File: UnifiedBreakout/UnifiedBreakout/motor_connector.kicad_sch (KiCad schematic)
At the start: 1 part, among them J7 RJ45

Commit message: WIP updating breakout for electrical enclosure
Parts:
- J7: symbol UnifiedBreakout-rescue:RJ45-Connector -> Connector:RJ45
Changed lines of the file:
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@@
-(kicad_sch (version 20211123) (generator eeschema)
+(kicad_sch (version 20230121) (generator eeschema)
   (paper "A4")
   (junction (at 121.92 92.71) (diameter 0.9144) (color 0 0 0 0)
@@
   )
   (wire (pts (xy 127 90.17) (xy 88.9 90.17))
-    (stroke (width 0) (type solid) (color 0 0 0 0))
+    (stroke (width 0) (type solid))
   )
   (wire (pts (xy 127 82.55) (xy 121.92 82.55))
-    (stroke (width 0) (type solid) (color 0 0 0 0))
+    (stroke (width 0) (type solid))
   )
   (wire (pts (xy 121.92 77.47) (xy 121.92 82.55))
-    (stroke (width 0) (type solid) (color 0 0 0 0))
+    (stroke (width 0) (type solid))
   )
   (wire (pts (xy 121.92 92.71) (xy 121.92 101.6))
-    (stroke (width 0) (type solid) (color 0 0 0 0))
+    (stroke (width 0) (type solid))
   )
   (wire (pts (xy 127 95.25) (xy 88.9 95.25))
-    (stroke (width 0) (type solid) (color 0 0 0 0))
+    (stroke (width 0) (type solid))
   )
   (wire (pts (xy 127 80.01) (xy 88.9 80.01))
-    (stroke (width 0) (type solid) (color 0 0 0 0))
+    (stroke (width 0) (type solid))
   )
   (wire (pts (xy 127 77.47) (xy 121.92 77.47))
-    (stroke (width 0) (type solid) (color 0 0 0 0))
+    (stroke (width 0) (type solid))
   )
   (wire (pts (xy 121.92 87.63) (xy 121.92 92.71))
-    (stroke (width 0) (type solid) (color 0 0 0 0))
+    (stroke (width 0) (type solid))
   )
   (wire (pts (xy 121.92 82.55) (xy 121.92 87.63))
-    (stroke (width 0) (type solid) (color 0 0 0 0))
+    (stroke (width 0) (type solid))
   )
   (wire (pts (xy 127 87.63) (xy 121.92 87.63))
-    (stroke (width 0) (type solid) (color 0 0 0 0))
+    (stroke (width 0) (type solid))
   )
   (wire (pts (xy 127 85.09) (xy 88.9 85.09))
-    (stroke (width 0) (type solid) (color 0 0 0 0))
+    (stroke (width 0) (type solid))
   )
   (wire (pts (xy 127 92.71) (xy 121.92 92.71))
-    (stroke (width 0) (type solid) (color 0 0 0 0))
+    (stroke (width 0) (type solid))
   )
-  (hierarchical_label "ENABLE" (shape input) (at 88.9 90.17 180)
+  (hierarchical_label "ENABLE" (shape input) (at 88.9 90.17 180) (fields_autoplaced)
     (effects (font (size 1.27 1.27)) (justify right))
   )
-  (hierarchical_label "ALARM" (shape input) (at 88.9 95.25 180)
+  (hierarchical_label "ALARM" (shape input) (at 88.9 95.25 180) (fields_autoplaced)
     (effects (font (size 1.27 1.27)) (justify right))
   )
-  (hierarchical_label "STEP" (shape input) (at 88.9 80.01 180)
+  (hierarchical_label "STEP" (shape input) (at 88.9 80.01 180) (fields_autoplaced)
     (effects (font (size 1.27 1.27)) (justify right))
   )
-  (hierarchical_label "DIR" (shape input) (at 88.9 85.09 180)
+  (hierarchical_label "DIR" (shape input) (at 88.9 85.09 180) (fields_autoplaced)
     (effects (font (size 1.27 1.27)) (justify right))
   )
-  (hierarchical_label "GND" (shape passive) (at 121.92 101.6 270)
+  (hierarchical_label "GND" (shape passive) (at 121.92 101.6 270) (fields_autoplaced)
     (effects (font (size 1.27 1.27)) (justify right))
   )
-  (symbol (lib_id "UnifiedBreakout-rescue:RJ45-Connector") (at 137.16 85.09 180) (unit 1)
-    (in_bom yes) (on_board yes)
-    (property "Reference" "J7" (id 0) (at 145.542 85.1916 0)
+  (symbol (lib_id "Connector:RJ45") (at 137.16 85.09 180) (unit 1)
+    (in_bom yes) (on_board yes) (dnp no)
+    (property "Reference" "J7" (at 145.542 85.1916 0)
       (effects (font (size 1.27 1.27)) (justify right))
     )
-    (property "Value" "RJ45" (id 1) (at 145.542 87.503 0)
+    (property "Value" "RJ45" (at 145.542 87.503 0)
       (effects (font (size 1.27 1.27)) (justify right))
     )
-    (property "Footprint" "Stewart:SS6488SANF1" (id 2) (at 137.16 85.725 90)
+    (property "Footprint" "Stewart:SS6488SANF1" (at 137.16 85.725 90)
       (effects (font (size 1.27 1.27)) hide)
     )
-    (property "Datasheet" "~" (id 3) (at 137.16 85.725 90)
+    (property "Datasheet" "~" (at 137.16 85.725 90)
       (effects (font (size 1.27 1.27)) hide)
     )
-    (property "MPN" "SS-6488S-A-NF-1" (id 4) (at 137.16 85.09 0)
+    (property "MPN" "SS-6488S-A-NF-1" (at 137.16 85.09 0)
       (effects (font (size 1.27 1.27)) hide)
     )
-    (property "Manufacturer" "Bel" (id 5) (at 137.16 85.09 0)
+    (property "Manufacturer" "Bel" (at 137.16 85.09 0)
+      (effects (font (size 1.27 1.27)) hide)
+    )
+    (property "Farnell PN" "" (at 137.16 85.09 0)
       (effects (font (size 1.27 1.27)) hide)
     )
@@
     (pin "7")
     (pin "8")
+    (instances
+      (project "UnifiedBreakout"
+        (path "/e63e39d7-6ac0-4ffd-8aa3-1841a4541b55/00000000-0000-0000-0000-00005e6754f3"
+          (reference "J7") (unit 1)
+        )
+        (path "/e63e39d7-6ac0-4ffd-8aa3-1841a4541b55/00000000-0000-0000-0000-00005e67fd54"
+          (reference "J8") (unit 1)
+        )
+        (path "/e63e39d7-6ac0-4ffd-8aa3-1841a4541b55/00000000-0000-0000-0000-00005e67ffe4"
+          (reference "J9") (unit 1)
+        )
+      )
+    )
   )
 )

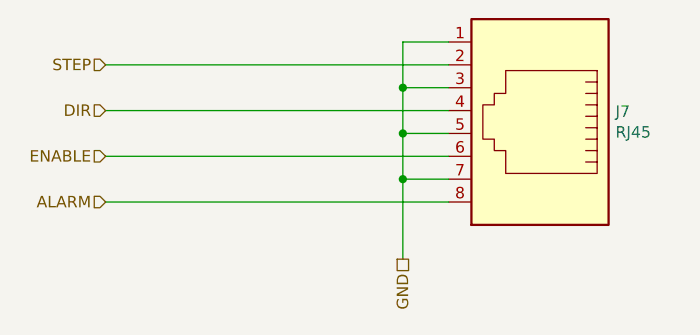
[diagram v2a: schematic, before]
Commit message: Grouped 4 way RJ45s
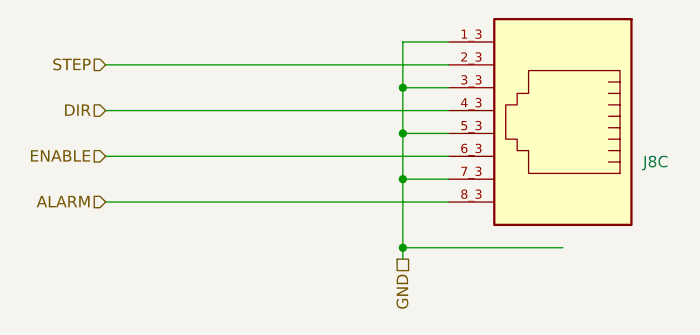
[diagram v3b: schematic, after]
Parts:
- removed J7: RJ45, Stewart:SS6488SANF1, symbol Connector:RJ45
- added J8: (no value), UnifiedBreakout:SS71800-041F, symbol UnifiedBreakout:SS71800-041F
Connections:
- net ALARM: now also J8.8_3 (P8_3)
- net DIR: now also J8.4_3 (P4_3)
- net ENABLE: now also J8.6_3 (P6_3)
- net GND: now also J8.1_3 (P1_3), J8.3_3 (P3_3), J8.5_3 (P5_3), J8.7_3 (P7_3)
- net STEP: now also J8.2_3 (P2_3)
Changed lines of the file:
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@@
   (junction (at 121.92 82.55) (diameter 0.9144) (color 0 0 0 0)
+  )
+  (junction (at 121.92 100.33) (diameter 0) (color 0 0 0 0)
   )
   (junction (at 121.92 87.63) (diameter 0.9144) (color 0 0 0 0)
@@
     (stroke (width 0) (type solid))
   )
-  (wire (pts (xy 121.92 92.71) (xy 121.92 101.6))
+  (wire (pts (xy 121.92 100.33) (xy 139.7 100.33))
+    (stroke (width 0) (type default))
+  )
+  (wire (pts (xy 121.92 92.71) (xy 121.92 100.33))
+    (stroke (width 0) (type solid))
+  )
+  (wire (pts (xy 121.92 100.33) (xy 121.92 101.6))
     (stroke (width 0) (type solid))
   )
@@
     (effects (font (size 1.27 1.27)) (justify right))
   )
-  (symbol (lib_id "Connector:RJ45") (at 137.16 85.09 180) (unit 1)
+  (symbol (lib_id "UnifiedBreakout:SS71800-041F") (at 139.7 86.36 0) (mirror y) (unit 3)
     (in_bom yes) (on_board yes) (dnp no)
-    (property "Reference" "J7" (at 145.542 85.1916 0)
+    (property "Reference" "J8" (at 148.59 90.805 0)
       (effects (font (size 1.27 1.27)) (justify right))
     )
-    (property "Value" "RJ45" (at 145.542 87.503 0)
+    (property "Value" "" (at 148.59 88.265 0)
       (effects (font (size 1.27 1.27)) (justify right))
     )
-    (property "Footprint" "Stewart:SS6488SANF1" (at 137.16 85.725 90)
+    (property "Footprint" "UnifiedBreakout:SS71800-041F" (at 139.7 86.36 0)
+      (effects (font (size 1.27 1.27)) (justify bottom) hide)
+    )
+    (property "Datasheet" "" (at 139.7 86.36 0)
       (effects (font (size 1.27 1.27)) hide)
     )
-    (property "Datasheet" "~" (at 137.16 85.725 90)
-      (effects (font (size 1.27 1.27)) hide)
+    (property "MPN" "SS71800-041F" (at 148.59 85.725 0)
+      (effects (font (size 1.27 1.27)) (justify right) hide)
     )
-    (property "MPN" "SS-6488S-A-NF-1" (at 137.16 85.09 0)
-      (effects (font (size 1.27 1.27)) hide)
+    (property "Manufacturer" "Stewart Connector" (at 148.59 83.185 0)
+      (effects (font (size 1.27 1.27)) (justify right) hide)
     )
-    (property "Manufacturer" "Bel" (at 137.16 85.09 0)
-      (effects (font (size 1.27 1.27)) hide)
+    (property "Farnell PN" "2891045" (at 148.59 80.645 0)
+      (effects (font (size 1.27 1.27)) (justify right) hide)
     )
-    (property "Farnell PN" "" (at 137.16 85.09 0)
-      (effects (font (size 1.27 1.27)) hide)
-    )
-    (pin "1")
-    (pin "2")
-    (pin "3")
-    (pin "4")
-    (pin "5")
-    (pin "6")
-    (pin "7")
-    (pin "8")
+    (pin "1_1")
+    (pin "2_1")
+    (pin "3_1")
+    (pin "4_1")
+    (pin "5_1")
+    (pin "6_1")
+    (pin "7_1")
+    (pin "8_1")
+    (pin "S1")
+    (pin "S2")
+    (pin "S3")
+    (pin "S4")
+    (pin "S5")
+    (pin "1_2")
+    (pin "2_2")
+    (pin "3_2")
+    (pin "4_2")
+    (pin "5_2")
+    (pin "6_2")
+    (pin "7_2")
+    (pin "8_2")
+    (pin "1_3")
+    (pin "2_3")
+    (pin "3_3")
+    (pin "4_3")
+    (pin "5_3")
+    (pin "6_3")
+    (pin "7_3")
+    (pin "8_3")
+    (pin "1_4")
+    (pin "2_4")
+    (pin "3_4")
+    (pin "4_4")
+    (pin "5_4")
+    (pin "6_4")
+    (pin "7_4")
+    (pin "8_4")
     (instances
       (project "UnifiedBreakout"
-        (path "/e63e39d7-6ac0-4ffd-8aa3-1841a4541b55/00000000-0000-0000-0000-00005e6754f3"
-          (reference "J7") (unit 1)
+        (path "/e63e39d7-6ac0-4ffd-8aa3-1841a4541b55/00000000-0000-0000-0000-00005e67ffe4"
+          (reference "J8") (unit 3)
         )
         (path "/e63e39d7-6ac0-4ffd-8aa3-1841a4541b55/00000000-0000-0000-0000-00005e67fd54"
+          (reference "J8") (unit 2)
+        )
+        (path "/e63e39d7-6ac0-4ffd-8aa3-1841a4541b55/00000000-0000-0000-0000-00005e6754f3"
           (reference "J8") (unit 1)
         )
-        (path "/e63e39d7-6ac0-4ffd-8aa3-1841a4541b55/00000000-0000-0000-0000-00005e67ffe4"
-          (reference "J9") (unit 1)
-        )
       )

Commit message: Update IO and opto
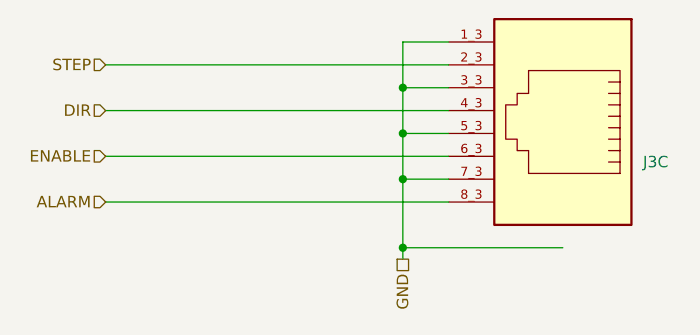
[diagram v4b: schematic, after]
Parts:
- J3: renamed from J8; value (none) -> ~
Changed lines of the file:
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@@
   (symbol (lib_id "UnifiedBreakout:SS71800-041F") (at 139.7 86.36 0) (mirror y) (unit 3)
     (in_bom yes) (on_board yes) (dnp no)
-    (property "Reference" "J8" (at 148.59 90.805 0)
+    (property "Reference" "J3" (at 148.59 90.805 0)
       (effects (font (size 1.27 1.27)) (justify right))
     )
-    (property "Value" "" (at 148.59 88.265 0)
+    (property "Value" "~" (at 148.59 88.265 0)
       (effects (font (size 1.27 1.27)) (justify right))
     )
@@
       (project "UnifiedBreakout"
         (path "/e63e39d7-6ac0-4ffd-8aa3-1841a4541b55/00000000-0000-0000-0000-00005e67ffe4"
-          (reference "J8") (unit 3)
+          (reference "J3") (unit 3)
         )
         (path "/e63e39d7-6ac0-4ffd-8aa3-1841a4541b55/00000000-0000-0000-0000-00005e67fd54"
-          (reference "J8") (unit 2)
+          (reference "J3") (unit 2)
         )
         (path "/e63e39d7-6ac0-4ffd-8aa3-1841a4541b55/00000000-0000-0000-0000-00005e6754f3"
-          (reference "J8") (unit 1)
+          (reference "J3") (unit 1)
         )
       )

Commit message: Started some layout
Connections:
- net ALARM: now also J3.8_2 (P8_2); no longer J3.8_3 (P8_3)
- net DIR: now also J3.4_2 (P4_2); no longer J3.4_3 (P4_3)
- net ENABLE: now also J3.6_2 (P6_2); no longer J3.6_3 (P6_3)
- net GND: now also J3.1_2 (P1_2), J3.3_2 (P3_2), J3.5_2 (P5_2), J3.7_2 (P7_2); no longer J3.1_3 (P1_3), J3.3_3 (P3_3), J3.5_3 (P5_3), J3.7_3 (P7_3)
- net STEP: now also J3.2_2 (P2_2); no longer J3.2_3 (P2_3)
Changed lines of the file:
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@@
     (effects (font (size 1.27 1.27)) (justify right))
   )
-  (symbol (lib_id "UnifiedBreakout:SS71800-041F") (at 139.7 86.36 0) (mirror y) (unit 3)
+  (symbol (lib_id "UnifiedBreakout:SS71800-041F") (at 139.7 86.36 0) (mirror y) (unit 2)
     (in_bom yes) (on_board yes) (dnp no)
     (property "Reference" "J3" (at 148.59 90.805 0)
@@
       (project "UnifiedBreakout"
         (path "/e63e39d7-6ac0-4ffd-8aa3-1841a4541b55/00000000-0000-0000-0000-00005e67ffe4"
+          (reference "J3") (unit 2)
+        )
+        (path "/e63e39d7-6ac0-4ffd-8aa3-1841a4541b55/00000000-0000-0000-0000-00005e67fd54"
           (reference "J3") (unit 3)
         )
-        (path "/e63e39d7-6ac0-4ffd-8aa3-1841a4541b55/00000000-0000-0000-0000-00005e67fd54"
-          (reference "J3") (unit 2)
-        )
         (path "/e63e39d7-6ac0-4ffd-8aa3-1841a4541b55/00000000-0000-0000-0000-00005e6754f3"
-          (reference "J3") (unit 1)
+          (reference "J3") (unit 4)
         )
       )

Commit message: Some layout
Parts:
- renumbered J3 to J4
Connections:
- net ALARM: now also J4.8_4 (P8_4); no longer J4.8_2 (P8_2)
- net DIR: now also J4.4_4 (P4_4); no longer J4.4_2 (P4_2)
- net ENABLE: now also J4.6_4 (P6_4); no longer J4.6_2 (P6_2)
- net GND: now also J4.1_4 (P1_4), J4.3_4 (P3_4), J4.5_4 (P5_4), J4.7_4 (P7_4); no longer J4.1_2 (P1_2), J4.3_2 (P3_2), J4.5_2 (P5_2), J4.7_2 (P7_2)
- net STEP: now also J4.2_4 (P2_4); no longer J4.2_2 (P2_2)
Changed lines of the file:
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@@
   (junction (at 121.92 82.55) (diameter 0.9144) (color 0 0 0 0)
-  )
-  (junction (at 121.92 100.33) (diameter 0) (color 0 0 0 0)
   )
   (junction (at 121.92 87.63) (diameter 0.9144) (color 0 0 0 0)
@@
     (stroke (width 0) (type solid))
   )
-  (wire (pts (xy 121.92 100.33) (xy 139.7 100.33))
-    (stroke (width 0) (type default))
-  )
-  (wire (pts (xy 121.92 92.71) (xy 121.92 100.33))
-    (stroke (width 0) (type solid))
-  )
-  (wire (pts (xy 121.92 100.33) (xy 121.92 101.6))
+  (wire (pts (xy 121.92 92.71) (xy 121.92 101.6))
     (stroke (width 0) (type solid))
   )
@@
     (effects (font (size 1.27 1.27)) (justify right))
   )
-  (symbol (lib_id "UnifiedBreakout:SS71800-041F") (at 139.7 86.36 0) (mirror y) (unit 2)
+  (symbol (lib_id "UnifiedBreakout:SS71800-041F") (at 139.7 86.36 0) (mirror y) (unit 4)
     (in_bom yes) (on_board yes) (dnp no)
-    (property "Reference" "J3" (at 148.59 90.805 0)
+    (property "Reference" "J4" (at 148.59 90.805 0)
       (effects (font (size 1.27 1.27)) (justify right))
     )
@@
       (project "UnifiedBreakout"
         (path "/e63e39d7-6ac0-4ffd-8aa3-1841a4541b55/00000000-0000-0000-0000-00005e67ffe4"
-          (reference "J3") (unit 2)
+          (reference "J4") (unit 4)
         )
         (path "/e63e39d7-6ac0-4ffd-8aa3-1841a4541b55/00000000-0000-0000-0000-00005e67fd54"
-          (reference "J3") (unit 3)
+          (reference "J4") (unit 3)
         )
         (path "/e63e39d7-6ac0-4ffd-8aa3-1841a4541b55/00000000-0000-0000-0000-00005e6754f3"
-          (reference "J3") (unit 4)
+          (reference "J4") (unit 2)
         )
       )
